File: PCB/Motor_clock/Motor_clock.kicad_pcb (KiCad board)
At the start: 2 copper layers, 111.8 x 73.7 mm, 54 parts, among them J1 WS2812, J10 M_M_2, J11 USB_B_Micro, J2 Barrel_Jack_Switch, J3 Battery_input, J4 ICSP, J5 M_H_1, J6 M_S_1, J7 M_H_1, J8 M_S_2, J9 M_M_1, SW1 DS_reset, SW2 SW_Push, U1 DS3231M, U2 ATmega328P-AU, U3 M_H_1, U4 M_S_1, U5 M_H_2, U6 M_S_2, U7 M_M_1, U8 M_M_2, U9 CH340G, Y1 16Mhz, Y2 12Mhz

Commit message: Bug fix
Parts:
- removed D4: LED, LED_SMD:LED_0603_1608Metric
- removed R10: 1k, Resistor_SMD:R_0603_1608Metric
- removed SW1: DS_reset, Button_Switch_SMD:SW_Push_1P1T_NO_6x6mm_H9.5mm
- added BZ1: Buzzer, Buzzer:buzzer, F.Cu at (145.0, 122.6)
- added C14: 100nF, Capacitor_SMD:C_0603_1608Metric, F.Cu at (128.6, 98.9)
- added C15: 100nF, Capacitor_SMD:C_0603_1608Metric, F.Cu at (157.1, 122.5)
- added G***: LOGO, picture:logo, B.Cu at (202.7, 116.3)
- added H1: MountingHole, MountingHole:MountingHole_3.2mm_M3, F.Cu at (208.4, 64.3)
- added H2: MountingHole, MountingHole:MountingHole_3.2mm_M3, F.Cu at (139.1, 60.6)
- added H3: MountingHole, MountingHole:MountingHole_3.2mm_M3, F.Cu at (215.3, 124.0)
- added H4: MountingHole, MountingHole:MountingHole_3.2mm_M3, F.Cu at (113.2, 124.5)
- added J12: Enc_M_2, Connector_JST:JST_PH_B4B-PH-K_1x04_P2.00mm_Vertical, F.Cu at (133.1, 58.8)
- added J13: Enc_H_2, Connector_JST:JST_PH_B4B-PH-K_1x04_P2.00mm_Vertical, F.Cu at (120.1, 58.8)
- added J14: Enc_S_2, Connector_JST:JST_PH_B4B-PH-K_1x04_P2.00mm_Vertical, F.Cu at (130.4, 71.9)
- added J15: Enc_S_1, Connector_JST:JST_PH_B4B-PH-K_1x04_P2.00mm_Vertical, F.Cu at (112.8, 70.7)
- added J16: Enc_M1, Connector_JST:JST_PH_B4B-PH-K_1x04_P2.00mm_Vertical, F.Cu at (126.6, 58.8)
- added J17: Enc_H_1, Connector_JST:JST_PH_B4B-PH-K_1x04_P2.00mm_Vertical, F.Cu at (113.7, 58.8)
- added Q1: Q_NPN_BEC, Package_TO_SOT_SMD:SOT-23, F.Cu at (158.0, 125.9)
- added U10: TCA9548APWR, Package_SO:TSSOP-24_4.4x7.8mm_P0.65mm, F.Cu at (130.5, 81.0)
- D3: value LED -> 1N5819; footprint LED_SMD:LED_0603_1608Metric -> Diode_SMD:D_SMA
- J1: footprint Connector_JST:JST_PH_B3B-PH-K_1x03_P2.00mm_Vertical -> Connector_JST:JST_XH_S3B-XH-A-1_1x03_P2.50mm_Horizontal
- J11: footprint Connector_USB:USB_Mini-B_AdamTech_MUSB-B5-S-VT-TSMT-1_SMD_Vertical -> USB:MicroXNJ
- L1: footprint Inductor_SMD:L_0603_1608Metric -> Inductor_SMD:L_Coilcraft_XAL5030
- moved D3 69.2 mm to (153.8, 124.5), turned to 270 degrees
- moved R9 69.0 mm to (159.0, 122.5), turned to 90 degrees
- moved C10 41.6 mm to (117.6, 106.7), turned to 0 degrees
- moved J11 41.0 mm to (114.4, 101.2), turned to 270 degrees
- moved D2 39.7 mm to (130.8, 106.0)
- moved C12 36.7 mm to (122.1, 106.6)
- moved C11 35.7 mm to (125.5, 106.6), turned to 0 degrees
- moved U9 32.3 mm to (121.4, 102.0), turned to 90 degrees
- moved Y2 29.4 mm to (129.1, 101.8), turned to 0 degrees
- moved C13 28.0 mm to (132.2, 101.8), turned to 270 degrees
- moved D1 20.8 mm to (113.3, 114.7), turned to 90 degrees
- moved SW2 18.3 mm to (117.3, 90.1)
- moved C9 18.0 mm to (116.0, 117.1), turned to 180 degrees
- moved C8 17.5 mm to (119.0, 116.1), turned to 270 degrees
- moved R8 15.5 mm to (116.0, 115.0), turned to 180 degrees
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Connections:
- BT1 pad 2: GND -> PDN
- C1 pad 2: GND -> PDN
- C10 pad 2: GND -> PDN
- C11 pad 2: GND -> PDN
- C12 pad 2: GND -> PDN
- C13 pad 2: GND -> PDN
- C2 pad 2: GND -> PDN
- C3 pad 1: GND -> PDN
- C4 pad 2: GND -> PDN
- C5 pad 2: GND -> PDN
- C6 pad 2: GND -> PDN
- C7 pad 2: GND -> PDN
- C9 pad 2: GND -> PDN
- D1 pad 1: GND -> PDN
- D3 pad 1: GND -> 12V
- D3 pad 2: Net-(D3-Pad2) -> Net-(BZ1-Pad2)
- J1 pad 3: GND -> PDN
- J11 pad 5: GND -> PDN
- J11 pad 6: GND -> PDN
- J2 pad 3: GND -> PDN
- J4 pad 6: GND -> PDN
- R7 pad 2: GND -> PDN
- R9 pad 1: TX -> Net-(Q1-Pad1)
- R9 pad 2: Net-(D3-Pad2) -> Buzzer
- SW2 pad 1: GND -> PDN
- U1 pad 10: GND -> PDN
- U1 pad 11: GND -> PDN
- U1 pad 12: GND -> PDN
- U1 pad 13: GND -> PDN
- U1 pad 4: Net-(SW1-Pad2) -> +5V
- U1 pad 5: GND -> PDN
- U1 pad 6: GND -> PDN
- U1 pad 7: GND -> PDN
- U1 pad 8: GND -> PDN
- U1 pad 9: GND -> PDN
- U2 pad 12: PDN -> Buzzer
- U2 pad 21: GND -> PDN
- U2 pad 3: GND -> PDN
- U2 pad 5: GND -> PDN
- U3 pad 1: GND -> PDN
- U3 pad 10: GND -> PDN
- U3 pad 16: GND -> PDN
- U3 pad 2: GND -> PDN
- U3 pad 3: GND -> PDN
- U4 pad 1: GND -> PDN
- U4 pad 10: GND -> PDN
- U4 pad 16: GND -> PDN
- U4 pad 2: GND -> PDN
- U4 pad 3: GND -> PDN
- U5 pad 1: GND -> PDN
- U5 pad 10: GND -> PDN
- U5 pad 16: GND -> PDN
- U5 pad 2: GND -> PDN
- U5 pad 3: GND -> PDN
- U6 pad 1: GND -> PDN
- U6 pad 10: GND -> PDN
- U6 pad 16: GND -> PDN
- U6 pad 2: GND -> PDN
- U6 pad 3: GND -> PDN
- U7 pad 1: GND -> PDN
- U7 pad 10: GND -> PDN
- U7 pad 16: GND -> PDN
- U7 pad 2: GND -> PDN
- U7 pad 3: GND -> PDN
- U8 pad 1: GND -> PDN
- U8 pad 10: GND -> PDN
- U8 pad 16: GND -> PDN
- U8 pad 2: GND -> PDN
- U8 pad 3: GND -> PDN
- U9 pad 1: GND -> PDN
- U9 pad 13: RESET -> Net-(C14-Pad1)
- VR1 pad 1: GND -> PDN
- Y1 pad 2: GND -> PDN
- Y1 pad 4: GND -> PDN
- Y2 pad 2: GND -> PDN
- Y2 pad 4: GND -> PDN
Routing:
- net PDN: track 165.7 -> 929.8 mm, vias 2 -> 11
- net GND: track 627.5 -> 0.00 mm, vias 3 -> 0
- net +5V: track 382.8 -> 544.5 mm
- net 12V: track 182.1 -> 224.7 mm, vias 2 -> 1
- net Buzzer: track 0.00 -> 40.9 mm
- net SC1: track 0.00 -> 29.7 mm, vias 0 -> 1
- net SC5: track 0.00 -> 29.2 mm, vias 0 -> 1
- net SC2: track 0.00 -> 28.1 mm, vias 0 -> 2
- net SD5: track 0.00 -> 27.4 mm, vias 0 -> 2
- net SCL: track 6.98 -> 32.8 mm
- net SD2: track 0.00 -> 25.1 mm, vias 0 -> 2
- net SD1: track 0.00 -> 24.2 mm, vias 0 -> 1
- net RX: track 39.7 -> 15.6 mm
- net SC4: track 0.00 -> 22.3 mm, vias 0 -> 1
- net SC3: track 0.00 -> 21.4 mm, vias 0 -> 1
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- added copper zone on B.Cu, net PDN
- removed copper zone on B.Cu, net GND
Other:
- board size 111.8 x 73.7 mm -> 111.8 x 74.7 mm
- board text added: "+"
- board text added: "H_1"
- board text added: "H_2"
- board text added: "M_1"
- board text added: "M_2"
- board text added: "S_1"
- board text added: "S_2"
- board text removed: "MOSI"
- board text removed: "SCK"

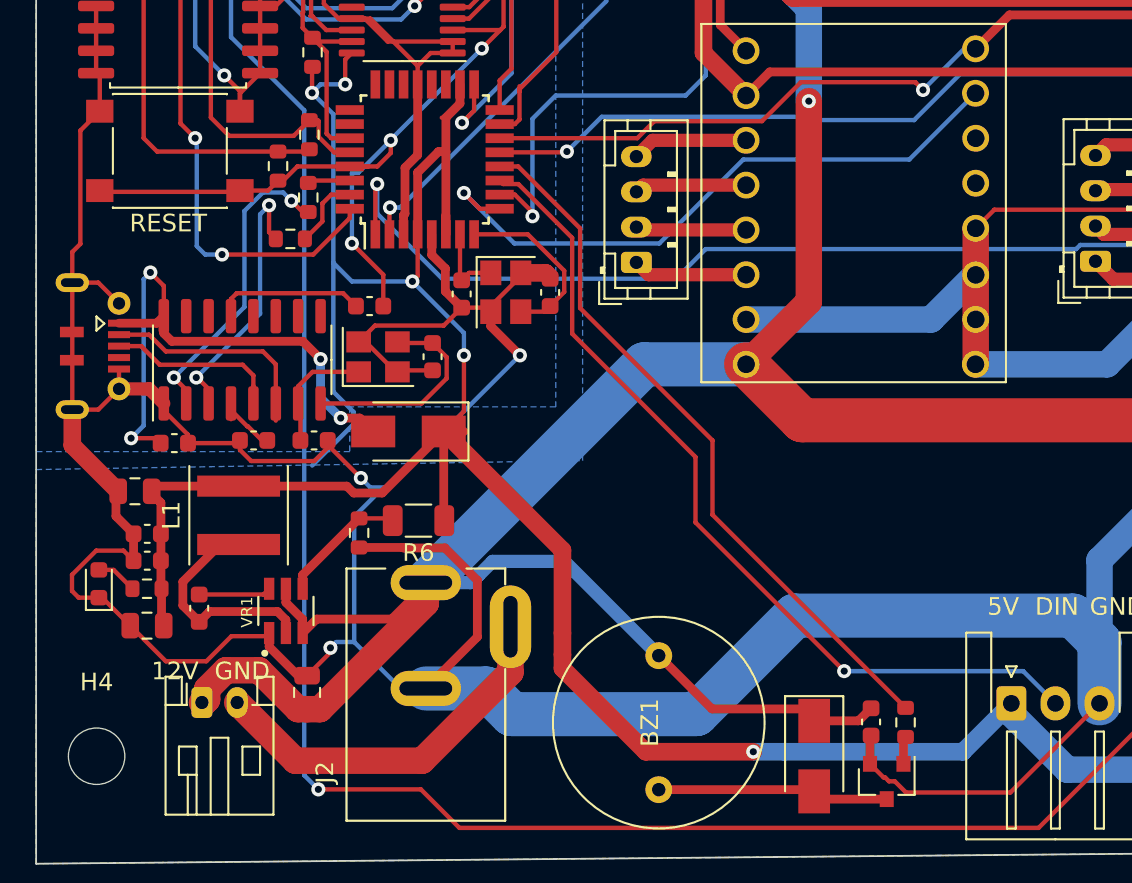
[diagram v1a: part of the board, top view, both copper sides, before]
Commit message: Change the inductor
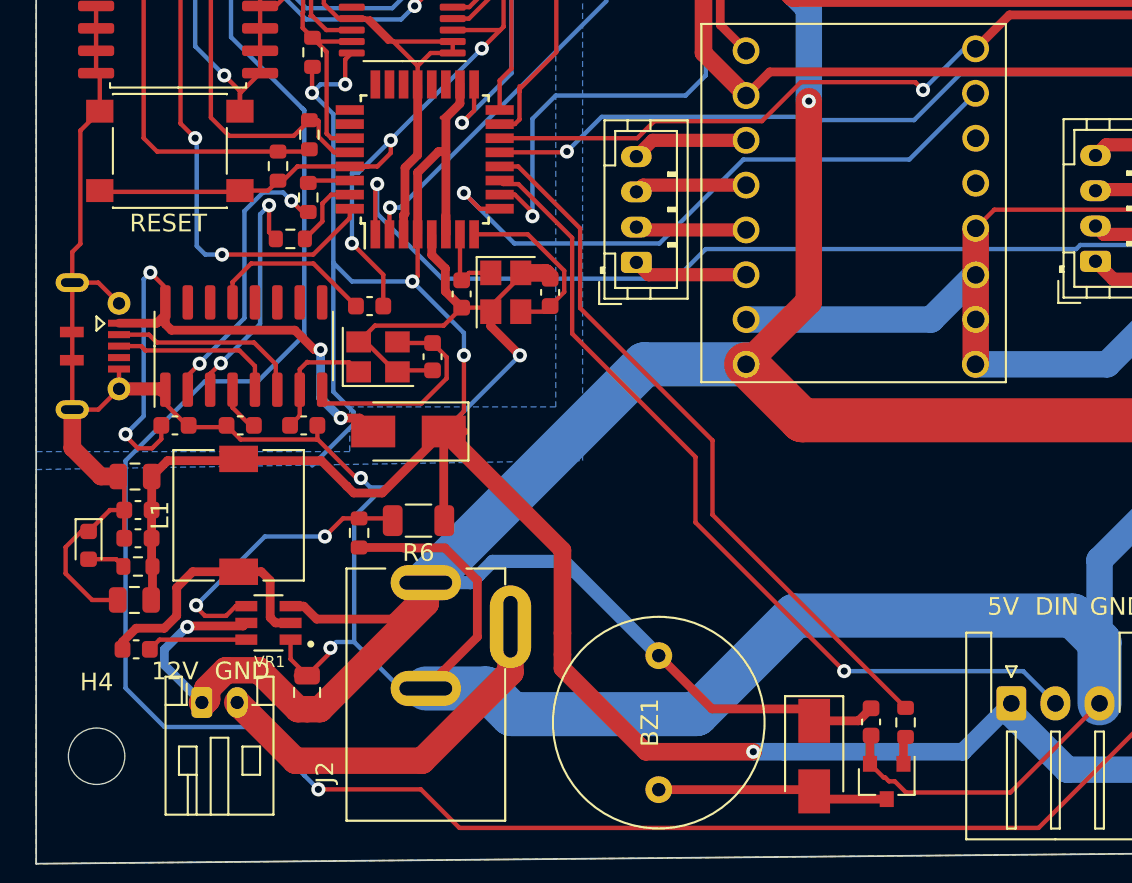
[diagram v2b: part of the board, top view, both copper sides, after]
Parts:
- L1: footprint Inductor_SMD:L_Coilcraft_XAL5030 -> Inductor_SMD:L_7.3x7.3_H4.5
- moved C8 4.27 mm to (115.4, 118.4), turned to 180 degrees
- moved D1 2.26 mm to (112.7, 112.5), turned to -90 degrees
- moved C9 1.62 mm to (115.3, 115.6)
- moved C4 1.45 mm to (115.5, 110.5)
- moved C2 1.38 mm to (115.5, 112.1)
- moved R8 1.36 mm to (115.5, 113.7)
- moved VR1 1.20 mm to (122.9, 116.9), turned to 180 degrees
- moved C12 1.14 mm to (121.3, 105.7)
- moved C11 1.04 mm to (124.9, 105.7)
- moved C10 1.01 mm to (117.6, 105.7)
- moved C5 0.84 mm to (115.3, 108.6)
- moved U9 0.78 mm to (121.5, 101.2)
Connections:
- J11 pad 4: (no net) -> unconnected-(J11-Pad4)
- U1 pad 1: (no net) -> unconnected-(U1-Pad1)
- U1 pad 3: (no net) -> unconnected-(U1-Pad3)
- U10 pad 17: (no net) -> unconnected-(U10-Pad17)
- U10 pad 18: (no net) -> unconnected-(U10-Pad18)
- U10 pad 19: (no net) -> unconnected-(U10-Pad19)
- U10 pad 20: (no net) -> unconnected-(U10-Pad20)
- U2 pad 19: (no net) -> unconnected-(U2-Pad19)
- U2 pad 20: (no net) -> unconnected-(U2-Pad20)
- U2 pad 22: (no net) -> unconnected-(U2-Pad22)
- U2 pad 23: (no net) -> unconnected-(U2-Pad23)
- U2 pad 24: (no net) -> unconnected-(U2-Pad24)
- U2 pad 25: (no net) -> unconnected-(U2-Pad25)
- U2 pad 26: (no net) -> unconnected-(U2-Pad26)
- U3 pad 5: (no net) -> unconnected-(U3-Pad5)
- U3 pad 6: (no net) -> unconnected-(U3-Pad6)
- U4 pad 5: (no net) -> unconnected-(U4-Pad5)
- U4 pad 6: (no net) -> unconnected-(U4-Pad6)
- U5 pad 5: (no net) -> unconnected-(U5-Pad5)
- U5 pad 6: (no net) -> unconnected-(U5-Pad6)
- U6 pad 5: (no net) -> unconnected-(U6-Pad5)
- U6 pad 6: (no net) -> unconnected-(U6-Pad6)
- U7 pad 5: (no net) -> unconnected-(U7-Pad5)
- U7 pad 6: (no net) -> unconnected-(U7-Pad6)
- U8 pad 5: (no net) -> unconnected-(U8-Pad5)
- U8 pad 6: (no net) -> unconnected-(U8-Pad6)
- U9 pad 10: (no net) -> unconnected-(U9-Pad10)
- U9 pad 11: (no net) -> unconnected-(U9-Pad11)
- U9 pad 12: (no net) -> unconnected-(U9-Pad12)
- U9 pad 14: (no net) -> unconnected-(U9-Pad14)
- U9 pad 15: (no net) -> unconnected-(U9-Pad15)
- U9 pad 9: (no net) -> unconnected-(U9-Pad9)
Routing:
- net Net-(BT1-Pad1): track 140.0 -> 153.7 mm
- net PDN: track 929.8 -> 916.8 mm
- net VFB: track 7.28 -> 16.6 mm, vias 0 -> 2
- net 12V: track 224.7 -> 232.2 mm, vias 1 -> 2
- net Net-(C8-Pad2): track 13.1 -> 15.7 mm
- net VBST: track 4.10 -> 5.70 mm
- net Net-(C14-Pad1): track 9.37 -> 10.9 mm
- net Net-(C11-Pad1): track 7.01 -> 8.24 mm
- net D+: track 10.9 -> 12.1 mm
- net D-: track 12.8 -> 11.8 mm
- net +5V: track 544.5 -> 545.4 mm
- net Net-(C12-Pad1): track 4.04 -> 3.46 mm
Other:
- net class Default removed
